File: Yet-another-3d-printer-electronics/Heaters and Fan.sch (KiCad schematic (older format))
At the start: 29 parts

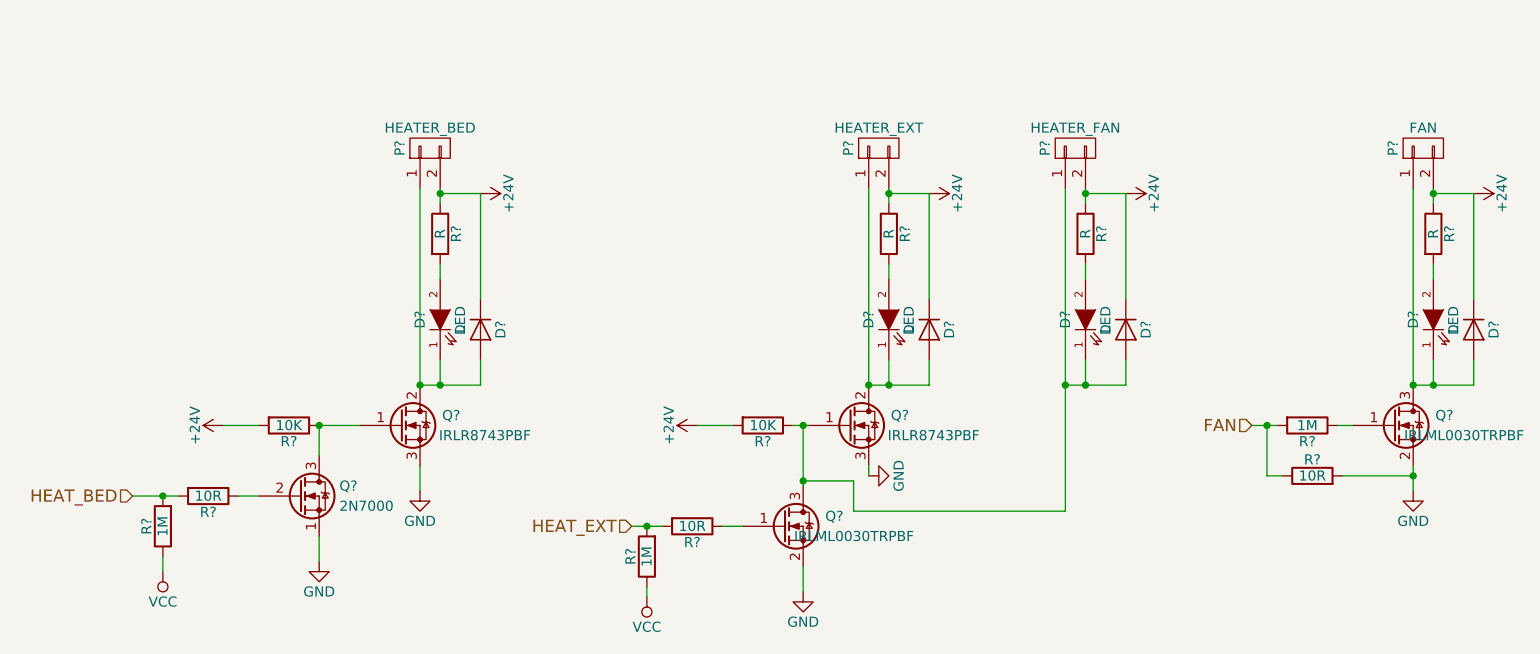
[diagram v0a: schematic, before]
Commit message: Add power section and remove fan heater
Add aoz1284pi buck conventer.

Signed-off-by: Mateusz Krawczuk <mat.krawczuk@gmail.com>
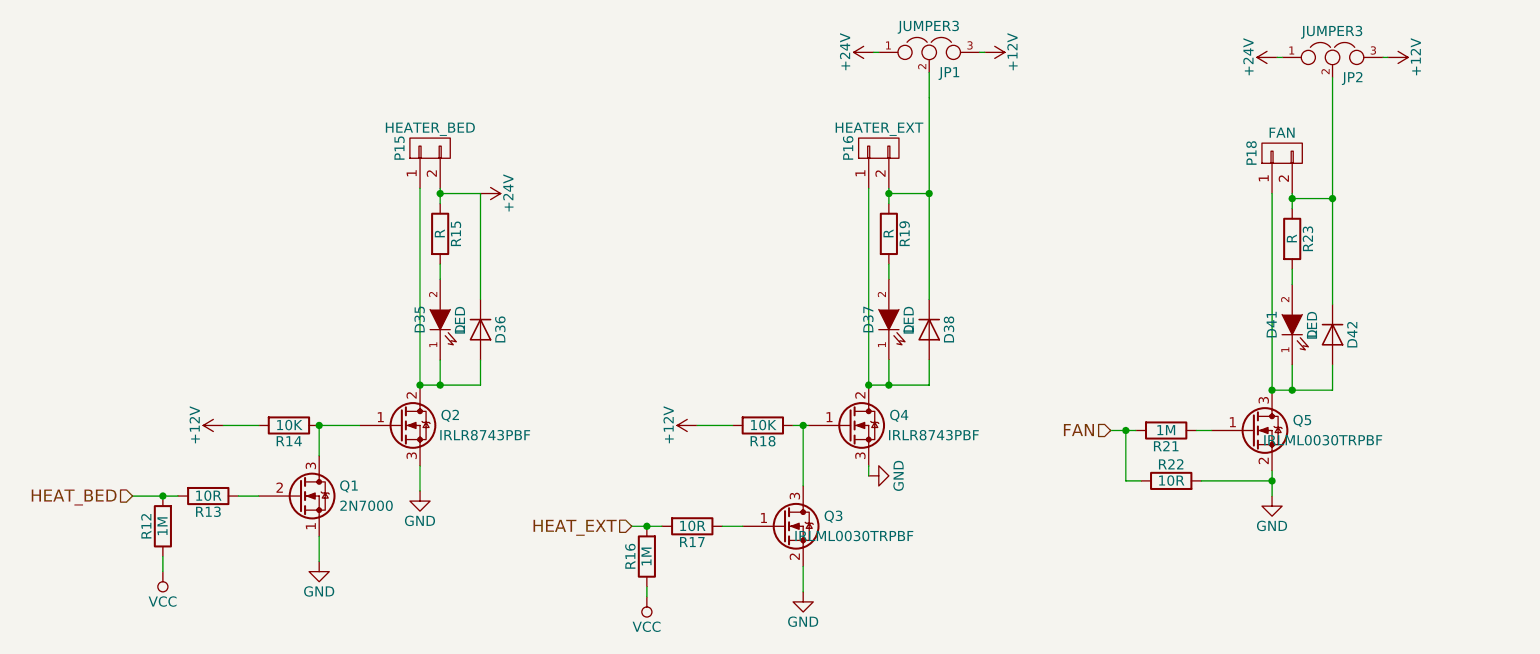
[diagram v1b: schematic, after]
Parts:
- removed D?: D, Diodes_THT:D_DO-41_SOD81_P2.54mm_Vertical_AnodeUp, symbol D
- removed D?: LED, LEDs:LED_0805, symbol LED-RESCUE-Yet-another-3d-printer-electronics
- removed P?: HEATER_FAN, Connectors_JST:JST_XH_B02B-XH-A_02x2.50mm_Straight, symbol CONN_01X02
- removed R?: R, Resistors_SMD:R_0805_HandSoldering, symbol R
- added JP1, JP2: JUMPER3, symbol JUMPER3
- gave numbers to parts that had none: 25
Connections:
- net +24V: now also JP1.1, JP2.1; no longer D38.1 (K), D42.1 (K), P16.2 (P2), P18.2 (P2), R14.2, R18.2, R19.1, R23.1
- new net: D42.1 (K), JP2.2, P18.2 (P2), R23.1
- new net: D38.1 (K), JP1.2, P16.2 (P2), R19.1
- new net +12V: JP1.3, JP2.3, R14.2, R18.2
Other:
- moved on the sheet: D41, D42, P18, Q5, R21, R22, R23

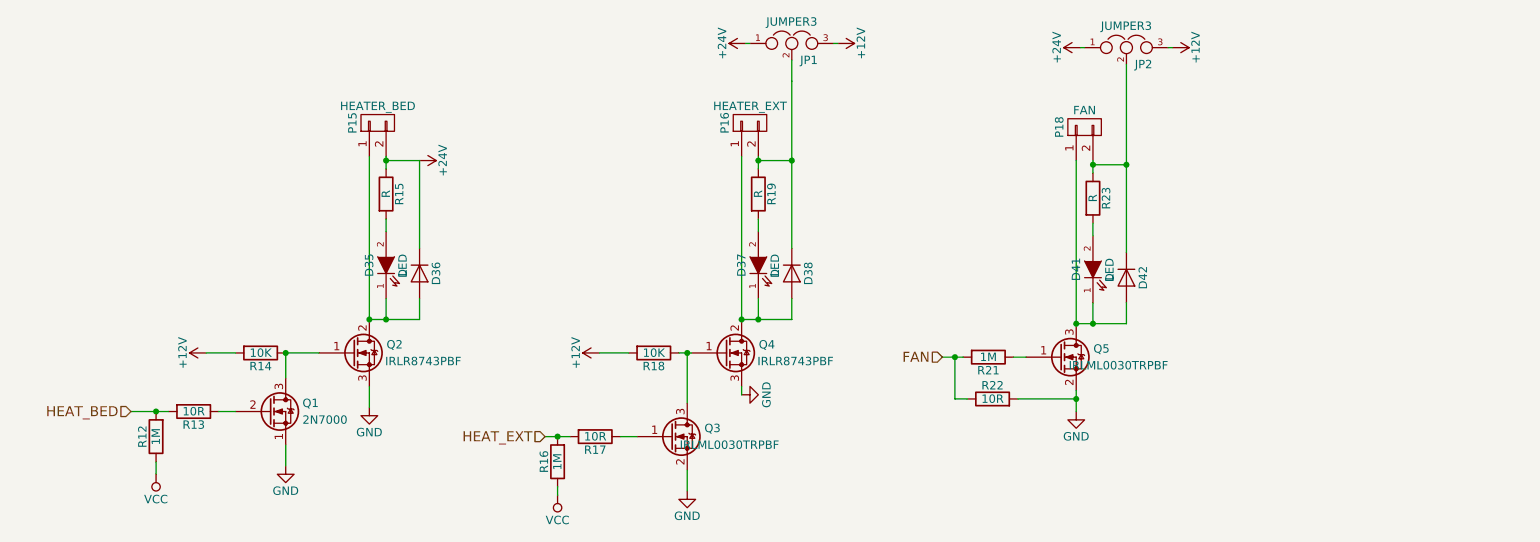
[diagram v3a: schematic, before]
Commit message: Add User_Fan
Additional Mosfet for second Fan or LED strip.

Signed-off-by: Mateusz Krawczuk <mat.krawczuk@gmail.com>
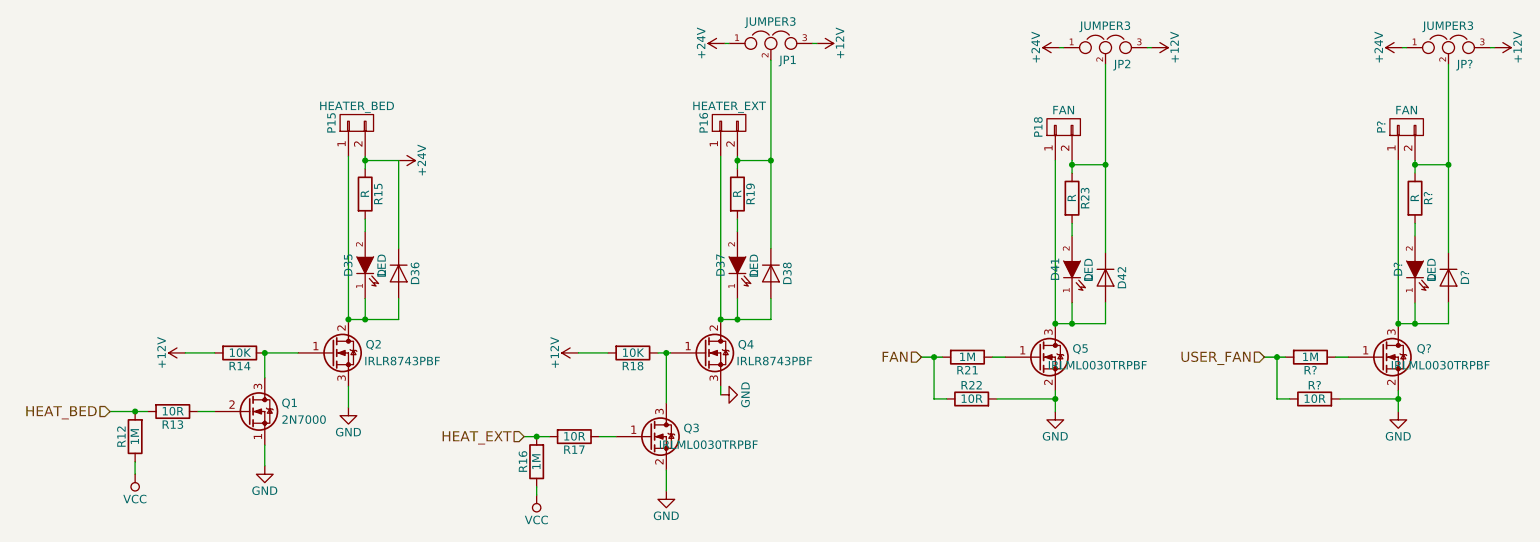
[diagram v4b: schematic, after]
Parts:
- added D?: D, Diodes_THT:D_DO-41_SOD81_P2.54mm_Vertical_AnodeUp, symbol D
- added D?: LED, LEDs:LED_0805, symbol LED-RESCUE-Yet-another-3d-printer-electronics
- added JP?: JUMPER3, symbol JUMPER3
- added P?: FAN, Connectors_JST:JST_XH_B02B-XH-A_02x2.50mm_Straight, symbol CONN_01X02
- added Q?: IRLML0030TRPBF, TO_SOT_Packages_SMD:SOT-23, symbol Q_NMOS_GSD
- added R?: R, Resistors_SMD:R_0805_HandSoldering, symbol R
- added R?: 1M, Resistors_SMD:R_0805_HandSoldering, symbol R
- added R?: 10R, Resistors_SMD:R_0805_HandSoldering, symbol R
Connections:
- net +12V: now also JP?.3
- net +24V: now also JP?.1
- net GND: now also Q?.2 (S), R?.2
- new net: D?.1 (K), D?.2 (A), P?.1 (P1), Q?.3 (D)
- new net: D?.1 (K), JP?.2, P?.2 (P2), R?.1
- new net: D?.2 (A), R?.2
- new net: Q?.1 (G), R?.1
- new net USER_FAN: R?.1, R?.2
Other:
- moved on the sheet: D35, D36, D37, D38, D41, D42, JP1, JP2, P15, P16, P18, Q1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

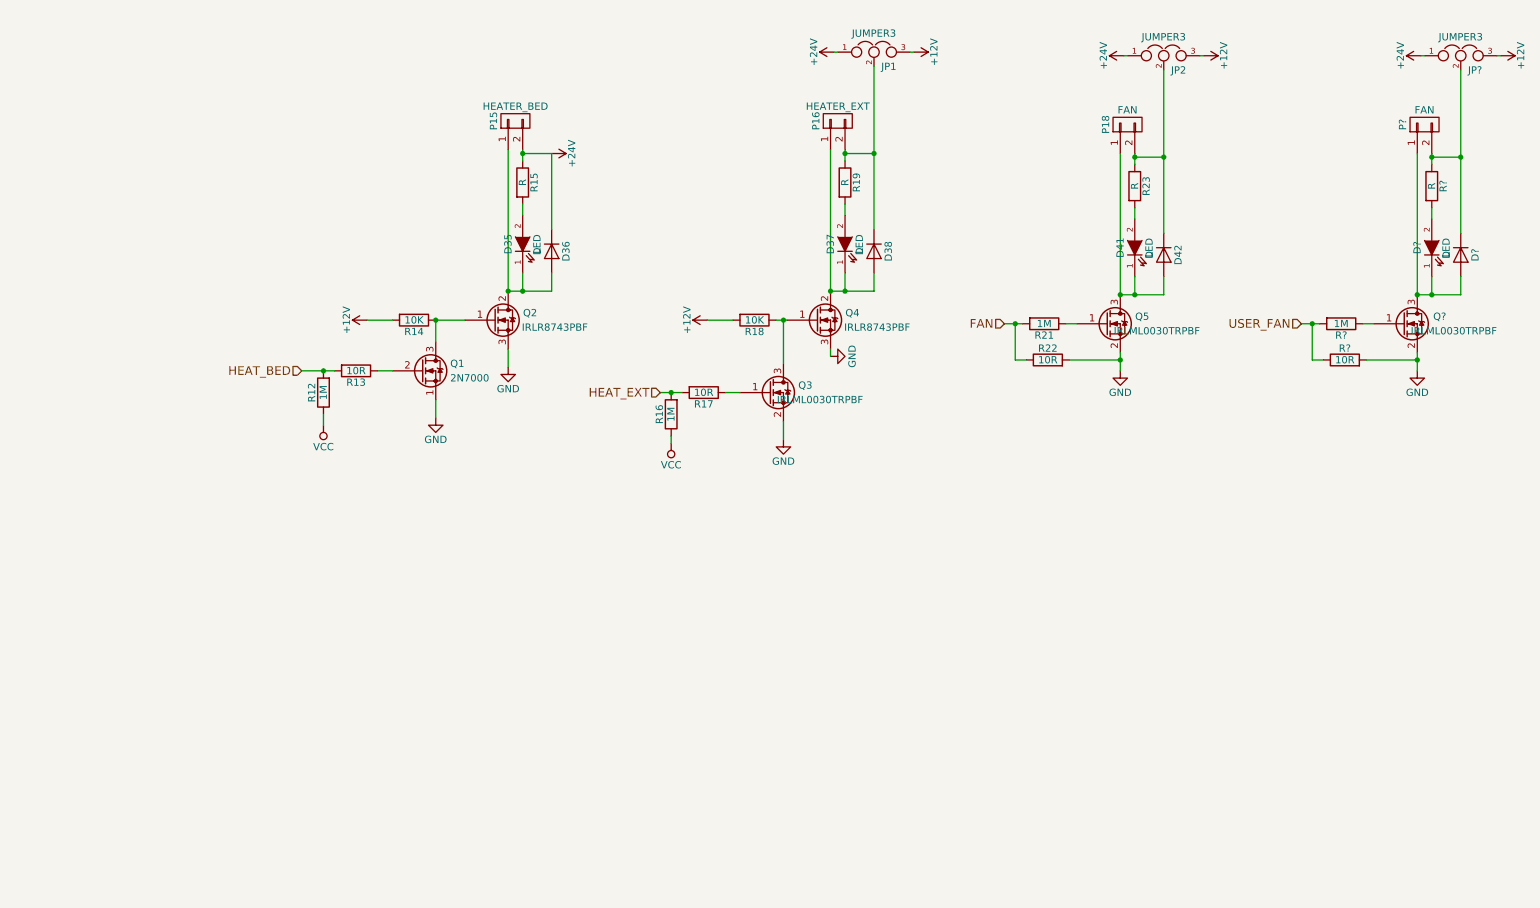
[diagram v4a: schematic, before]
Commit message: Add additional stepstick, hotend fan and heater and temperature sensor
Extruder stepsticks have independ enables pins. Vcc was replace by valid
power source.

Signed-off-by: Mateusz Krawczuk <mat.krawczuk@gmail.com>
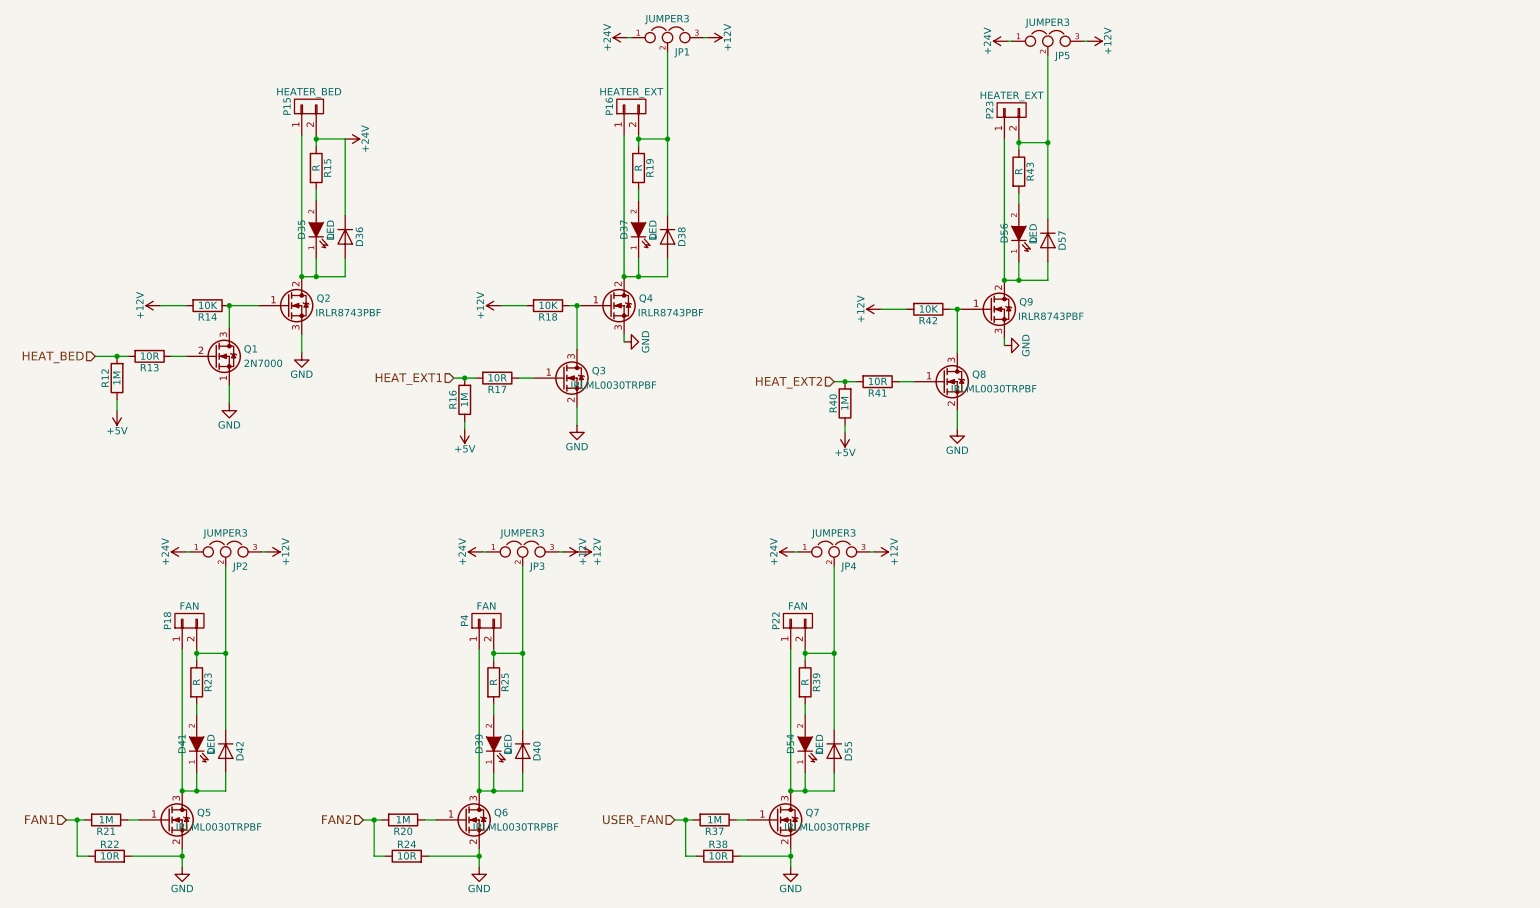
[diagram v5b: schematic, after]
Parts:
- added D54, D56: LED, LEDs:LED_0805, symbol LED-RESCUE-Yet-another-3d-printer-electronics
- added D55, D57: D, Diodes_THT:D_DO-41_SOD81_P2.54mm_Vertical_AnodeUp, symbol D
- added JP4, JP5: JUMPER3, symbol JUMPER3
- added P22: FAN, Connectors_JST:JST_XH_B02B-XH-A_02x2.50mm_Straight, symbol CONN_01X02
- added P23: HEATER_EXT, Connectors:AK300-2, symbol CONN_01X02
- added Q7, Q8: IRLML0030TRPBF, TO_SOT_Packages_SMD:SOT-23, symbol Q_NMOS_GSD
- added Q9: IRLR8743PBF, TO_SOT_Packages_SMD:TO-252-2Lead, symbol Q_NMOS_GDS
- added R37, R40: 1M, Resistors_SMD:R_0805_HandSoldering, symbol R
- added R38, R41: 10R, Resistors_SMD:R_0805_HandSoldering, symbol R
- added R39, R43: R, Resistors_SMD:R_0805_HandSoldering, symbol R
- added R42: 10K, Resistors_SMD:R_0805_HandSoldering, symbol R
- gave numbers to parts that had none: 8
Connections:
- net +12V: now also JP4.3, JP5.3, R42.2
- net +24V: now also JP4.1, JP5.1
- net GND: now also Q7.2 (S), Q8.2 (S), Q9.3 (S), R38.2
- net USER_FAN: now also R37.2, R38.1; no longer R20.2, R24.1
- net FAN renamed FAN1
- net HEAT_EXT renamed HEAT_EXT1
- net VCC renamed +5V
- net +5V: now also R40.1
- new net: D54.1 (K), D55.2 (A), P22.1 (P1), Q7.3 (D)
- new net: D55.1 (K), JP4.2, P22.2 (P2), R39.1
- new net: D54.2 (A), R39.2
- new net: Q7.1 (G), R37.1
- new net: D56.1 (K), D57.2 (A), P23.1 (P1), Q9.2 (D)
- new net: D57.1 (K), JP5.2, P23.2 (P2), R43.1
- new net: Q8.3 (D), Q9.1 (G), R42.1
- new net: D56.2 (A), R43.2
- new net: Q8.1 (G), R41.1
- new net FAN2: R20.2, R24.1
- new net HEAT_EXT2: R40.2, R41.2
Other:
- moved on the sheet: D35, D36, D37, D38, D39, D40, D41, D42, JP1, JP2, JP3, P15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

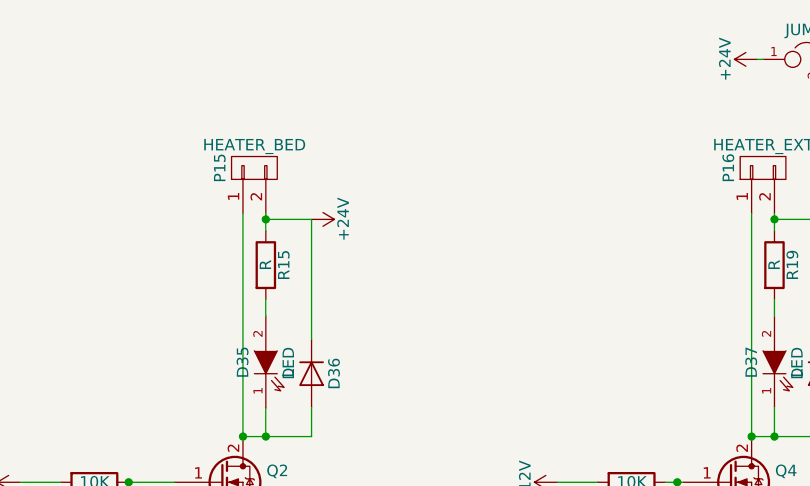
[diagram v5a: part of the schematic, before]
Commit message: Add fuses to powersupply connector and heatbed.
TVS diode used to protect pins from short circuit. Correct connectors
names.

Signed-off-by: Mateusz Krawczuk <mat.krawczuk@gmail.com>
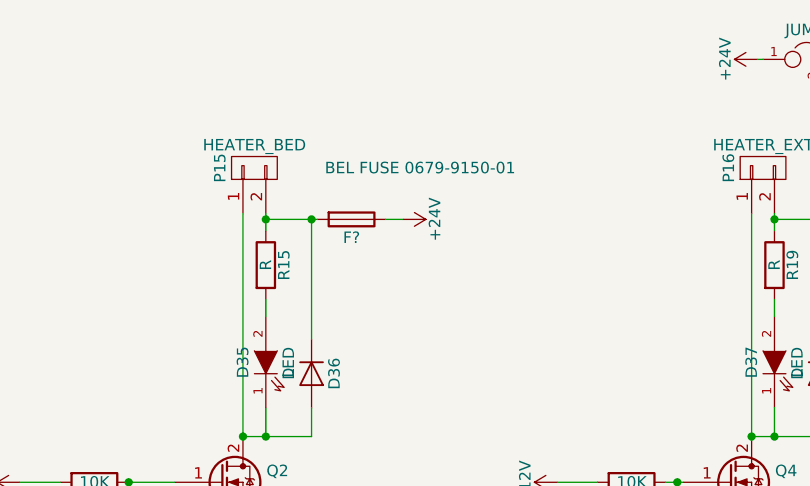
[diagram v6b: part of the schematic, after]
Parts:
- added F?: BEL FUSE 0679-9150-01, symbol Fuse
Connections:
- net +24V: now also F?.1; no longer D36.1 (K), P15.2 (P2), R15.1
- new net: D36.1 (K), F?.2, P15.2 (P2), R15.1
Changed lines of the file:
@@
 L +24V #PWR0107
 U 1 1 58B2B483
-P 2800 1850
-F 0 "#PWR0107" H 2800 1700 50  0001 C CNN
-F 1 "+24V" H 2800 1990 50  0000 C CNN
-F 2 "" H 2800 1850 50  0000 C CNN
-F 3 "" H 2800 1850 50  0000 C CNN
-	1    2800 1850
+P 3200 1850
+F 0 "#PWR0107" H 3200 1700 50  0001 C CNN
+F 1 "+24V" H 3200 1990 50  0000 C CNN
+F 2 "" H 3200 1850 50  0000 C CNN
+F 3 "" H 3200 1850 50  0000 C CNN
+	1    3200 1850
 	0    1    1    0
 $EndComp
@@
 Connection ~ 2600 1850
 Wire Wire Line
-	2800 1850 2600 1850
+	2600 1850 2825 1850
 Connection ~ 2600 2800
 Wire Wire Line
@@
 	-1   0    0    1
 $EndComp
+$Comp
+L Fuse F?
+U 1 1 5903EAF9
+P 2975 1850
+F 0 "F?" V 3055 1850 50  0000 C CNN
+F 1 "BEL FUSE 0679-9150-01" V 2750 2150 50  0000 C CNN
+F 2 "" V 2905 1850 50  0001 C CNN
+F 3 "" H 2975 1850 50  0001 C CNN
+	1    2975 1850
+	0    1    1    0
+$EndComp
+Wire Wire Line
+	3200 1850 3125 1850
+Connection ~ 2800 1850
 $EndSCHEMATC
